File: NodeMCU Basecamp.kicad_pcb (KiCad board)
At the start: 2 copper layers, 71.1 x 53.3 mm, 60 parts, among them Q1 BSS138, Q10 BSS138, Q11 BSS138, Q12 BSS138, Q13 BSS138, Q2 BSS138, Q3 BSS138, Q4 BSS138, Q5 BSS138, Q6 BSS138, Q7 BSS138, Q8 BSS138, Q9 BSS138, U1 GND_BUS, U10 S_JUMPER_4, U11 S_JUMPER_4, U12 S_JUMPER_4, U13 S_JUMPER_4, U14 S_JUMPER_4, U15 S_JUMPER_4, U16 S_JUMPER_4, U17 S_JUMPER_4, U18 S_JUMPER_4, U19 S_JUMPER_4, U2 NODEMCU_AMICA, U3 DEV_PINS, U4 3V3_BUS, U5 5V_BUS, U6 S_JUMPER_4, U7 S_JUMPER_4, U8 S_JUMPER_4, U9 S_JUMPER_4

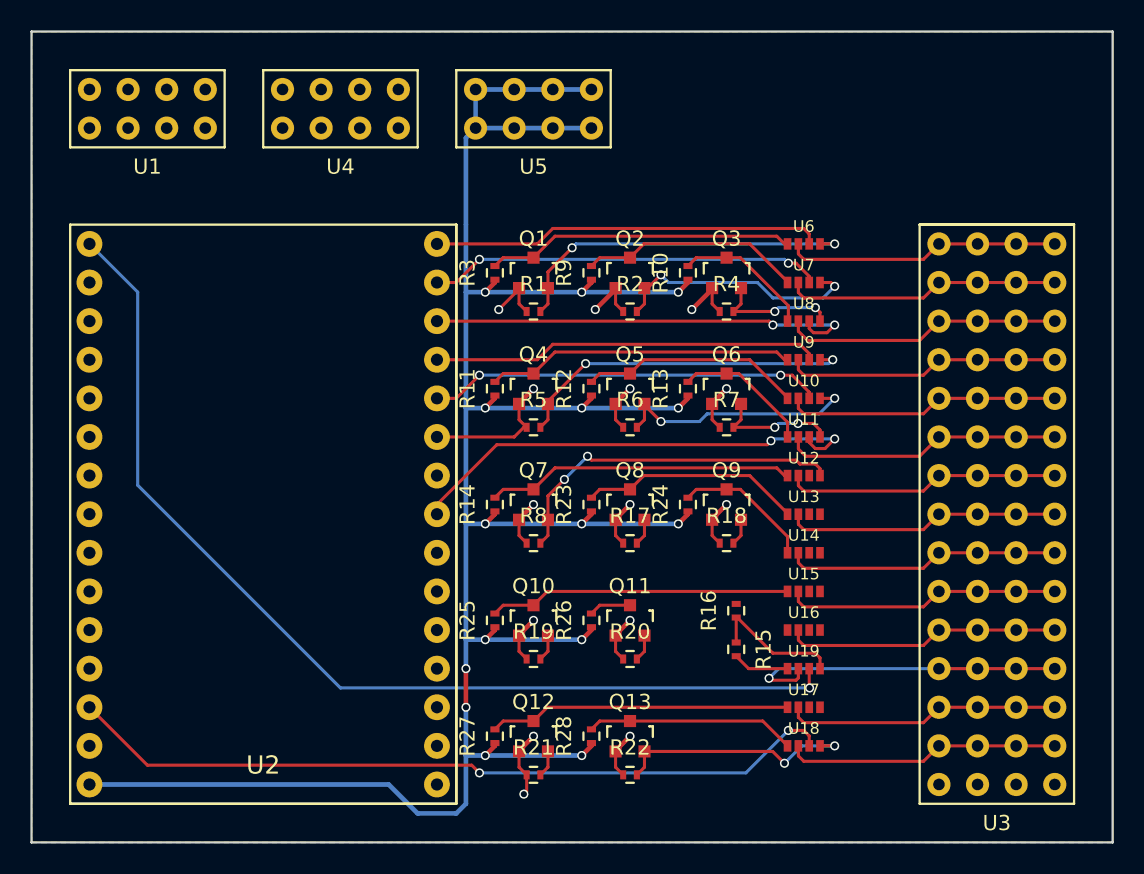
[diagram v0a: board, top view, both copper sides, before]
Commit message: rework: remove jumpers
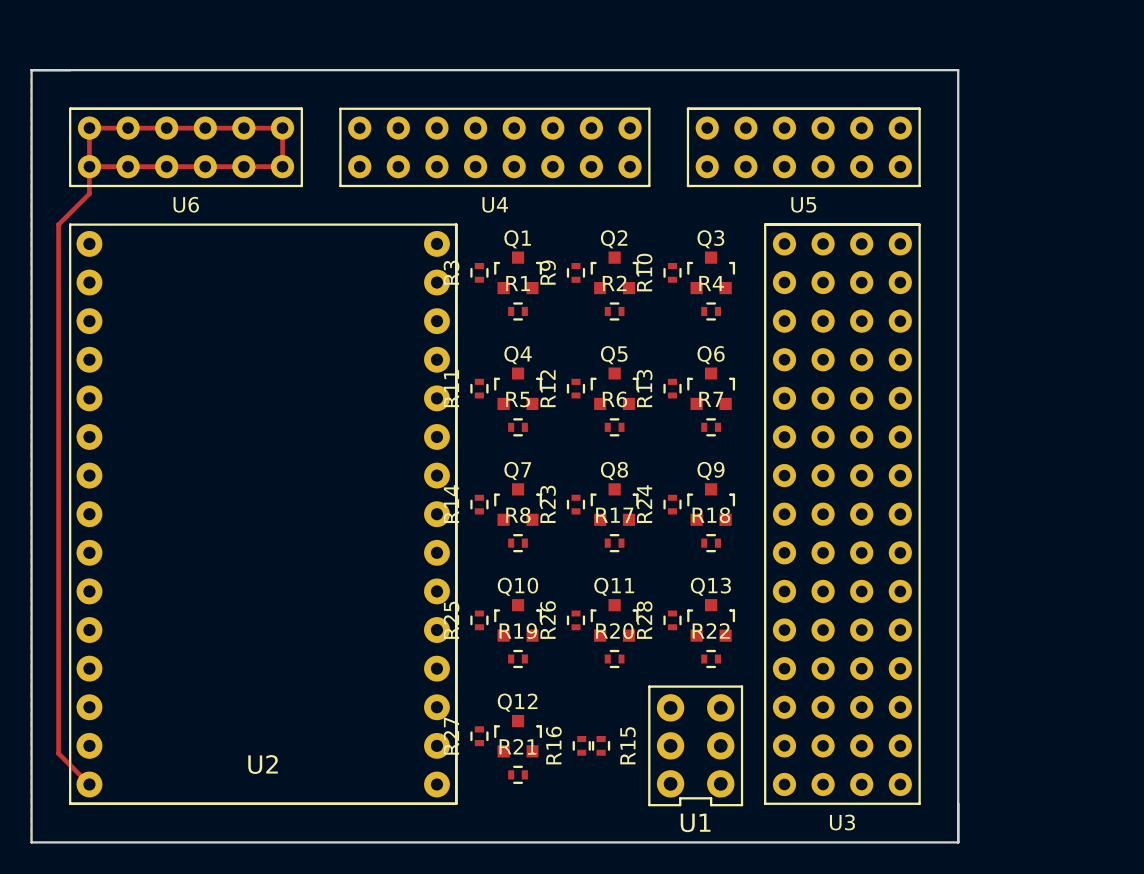
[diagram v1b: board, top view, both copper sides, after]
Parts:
- removed U10, U11, U12, U13, U14, U15, U16, U17, U18, U19, U7, U8, U9: S_JUMPER_4, mplewis:S_JUMPER_4
- Q1: footprint SOT-23 -> TO_SOT_Packages_SMD:SOT-23
- R15: value 33K -> 10K
- R16: value 68K -> 10K
- R21: value 10K -> 33K
- R22: value 10K -> 68K
- U1: value GND_BUS -> JS202011CQN; footprint mplewis:HEADER_BUS_4X2 -> mplewis:JS202011CQN
- U4: value 3V3_BUS -> GND_BUS; footprint mplewis:HEADER_BUS_4X2 -> mplewis:HEADER_BUS_4X8
- U5: value 5V_BUS -> 3V3_BUS; footprint mplewis:HEADER_BUS_4X2 -> mplewis:HEADER_BUS_4X6
- U6: value S_JUMPER_4 -> 5V_BUS; footprint mplewis:S_JUMPER_4 -> mplewis:HEADER_BUS_4X6
- moved U1 55.3 mm to (69.1, 69.8), turned to 180 degrees
- moved U6 41.1 mm to (35.6, 30.5)
- moved U5 18.0 mm to (76.2, 30.5)
- moved R16 13.5 mm to (61.6, 69.8)
- moved R15 10.9 mm to (62.9, 69.8)
- moved U4 10.5 mm to (55.9, 30.5)
- moved U3 10.2 mm to (78.7, 54.6)
- moved Q13 9.30 mm to (70.1, 61.6)
- moved R28 9.30 mm to (67.6, 61.6)
- moved R22 9.30 mm to (70.1, 64.1)
- moved Q3 1.02 mm to (70.1, 38.7)
- moved Q6 1.02 mm to (70.1, 46.4)
- moved Q9 1.02 mm to (70.1, 54.0)
- moved R10 1.02 mm to (67.6, 38.7)
- moved R11 1.02 mm to (54.9, 46.4)
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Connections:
- Q1 pad 2: D0_LV_LT -> D0_LV
- Q1 pad 3: D0_HV -> D0_XV
- Q10 pad 2: RX_LV_LT -> RX_LV
- Q10 pad 3: RX_HV -> RX_XV
- Q11 pad 2: TX_LV_LT -> TX_LV
- Q11 pad 3: TX_HV -> TX_XV
- Q12 pad 2: EN_LV_LT -> EN_LV
- Q12 pad 3: EN_HV -> EN_XV
- Q13 pad 2: RST_LV_LT -> RST_LV
- Q13 pad 3: RST_HV -> RST_XV
- Q2 pad 2: D1_LV_LT -> D1_LV
- Q2 pad 3: D1_HV -> D1_XV
- Q3 pad 2: D2_LV_LT -> D2_LV
- Q3 pad 3: D2_HV -> D2_XV
- Q4 pad 2: D3_LV_LT -> D3_LV
- Q4 pad 3: D3_HV -> D3_XV
- Q5 pad 2: D4_LV_LT -> D4_LV
- Q5 pad 3: D4_HV -> D4_XV
- Q6 pad 2: D5_LV_LT -> D5_LV
- Q6 pad 3: D5_HV -> D5_XV
- Q7 pad 2: D6_LV_LT -> D6_LV
- Q7 pad 3: D6_HV -> D6_XV
- Q8 pad 2: D7_LV_LT -> D7_LV
- Q8 pad 3: D7_HV -> D7_XV
- Q9 pad 2: D8_LV_LT -> D8_LV
- Q9 pad 3: D8_HV -> D8_XV
- R1 pad 2: D0_LV_LT -> D0_LV
- R10 pad 1: 5V -> OP_V
- R10 pad 2: D2_HV -> D2_XV
- R11 pad 1: 5V -> OP_V
- R11 pad 2: D3_HV -> D3_XV
- R12 pad 1: 5V -> OP_V
- R12 pad 2: D4_HV -> D4_XV
- R13 pad 1: 5V -> OP_V
- R13 pad 2: D5_HV -> D5_XV
- R14 pad 1: 5V -> OP_V
- R14 pad 2: D6_HV -> D6_XV
- R15 pad 1: A0_LV_LT -> 3V3
- R15 pad 2: A0_HV -> D7_LV
- R16 pad 1: A0_LV_LT -> 3V3
- R16 pad 2: GND -> D8_LV
- R17 pad 2: D7_LV_LT -> RX_LV
- R18 pad 2: D8_LV_LT -> TX_LV
- R19 pad 2: RX_LV_LT -> EN_LV
- R2 pad 2: D1_LV_LT -> D1_LV
- R20 pad 2: TX_LV_LT -> RST_LV
- R21 pad 1: 3V3 -> A0_LV_LT
- R21 pad 2: EN_LV_LT -> (no net)
- R22 pad 1: 3V3 -> A0_LV_LT
- R22 pad 2: RST_LV_LT -> Earth
- R23 pad 1: 5V -> OP_V
- R23 pad 2: D7_HV -> D7_XV
- R24 pad 1: 5V -> OP_V
- R24 pad 2: D8_HV -> D8_XV
- R25 pad 1: 5V -> OP_V
- R25 pad 2: RX_HV -> RX_XV
- R26 pad 1: 5V -> OP_V
- R26 pad 2: TX_HV -> TX_XV
- R27 pad 1: 5V -> OP_V
- R27 pad 2: EN_HV -> EN_XV
- R28 pad 1: 5V -> OP_V
- R28 pad 2: RST_HV -> RST_XV
- R3 pad 1: 5V -> 3V3
- R3 pad 2: D0_HV -> D2_LV
- R4 pad 2: D2_LV_LT -> D3_LV
- R5 pad 2: D3_LV_LT -> D4_LV
- R6 pad 2: D4_LV_LT -> D5_LV
- R7 pad 2: D5_LV_LT -> D6_LV
- R8 pad 1: 3V3 -> OP_V
- R8 pad 2: D6_LV_LT -> D0_XV
- R9 pad 1: 5V -> (no net)
- R9 pad 2: D1_HV -> D1_XV
- U1 pad 1: GND -> 3V3
- U2 pad 1: A0_LV -> (no net)
- U2 pad 10: GND -> Earth
- U2 pad 14: GND -> Earth
- U2 pad 17: GND -> Earth
- U2 pad 2: Net-(U2-Pad2) -> (no net)
- U2 pad 24: GND -> Earth
- U2 pad 3: Net-(U2-Pad3) -> (no net)
- U2 pad 4: Net-(U2-Pad4) -> (no net)
- U2 pad 5: Net-(U2-Pad5) -> (no net)
- U2 pad 6: Net-(U2-Pad6) -> (no net)
- U2 pad 7: Net-(U2-Pad7) -> (no net)
- U2 pad 8: Net-(U2-Pad8) -> (no net)
- U2 pad 9: Net-(U2-Pad9) -> (no net)
- U3 pad 15: GND -> Earth
- U4 pad 1: 3V3 -> Earth
- U5 pad 1: 5V -> 3V3
- U6 pad 1: D0_HV -> 5V
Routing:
- net 5V: track 159.5 -> 72.8 mm, vias 15 -> 0
- net A0_LV: track 68.2 -> 0.00 mm, vias 1 -> 0
- net RST_LV: track 51.1 -> 0.00 mm, vias 2 -> 0
- net 3V3: track 50.2 -> 0.00 mm, vias 14 -> 0
- net D5_LV: track 31.0 -> 0.00 mm, vias 2 -> 0
- net D2_LV: track 28.8 -> 0.00 mm, vias 2 -> 0
- net D4_LV: track 26.0 -> 0.00 mm, vias 2 -> 0
- net D1_LV: track 26.0 -> 0.00 mm, vias 2 -> 0
- net D0_LV: track 25.7 -> 0.00 mm
- net D3_LV: track 25.6 -> 0.00 mm
- net D0_LV_LT: track 23.4 -> 0.00 mm, vias 2 -> 0
- net D6_LV_LT: track 23.1 -> 0.00 mm, vias 2 -> 0
- net D3_LV_LT: track 22.6 -> 0.00 mm, vias 2 -> 0
- net A0_XV: track 21.7 -> 0.00 mm, vias 1 -> 0
- net D6_HV: track 20.3 -> 0.00 mm
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- added copper zone on F.Cu, net Earth
- removed copper zone on F.Cu, net GND
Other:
- board size 71.1 x 53.3 mm -> 61 x 50.8 mm

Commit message: pcb: LT wired to dev pins
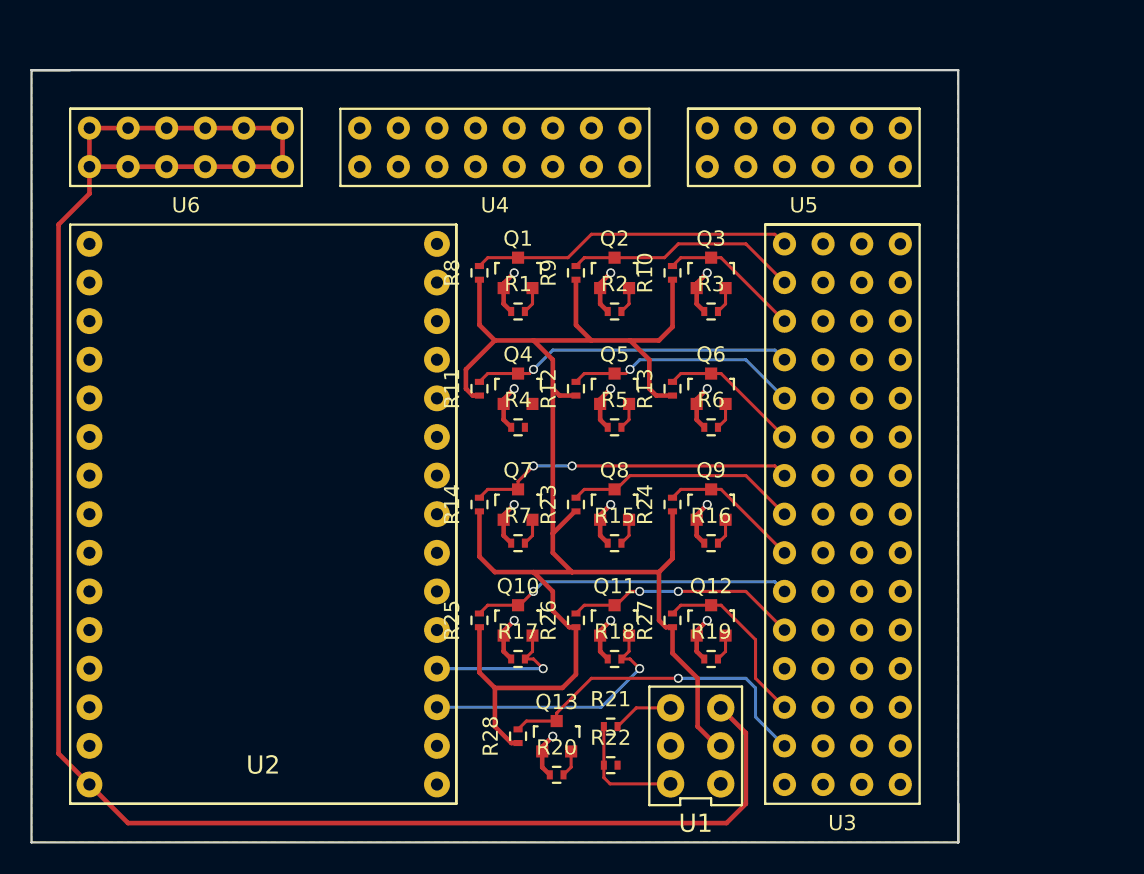
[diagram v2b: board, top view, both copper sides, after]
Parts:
- moved R8 18.0 mm to (54.9, 38.7), turned to 90 degrees
- moved R16 15.8 mm to (70.1, 56.5), turned to 0 degrees
- moved R3 15.5 mm to (70.1, 41.3), turned to 0 degrees
- moved Q12 14.8 mm to (70.1, 61.6)
- moved R27 14.8 mm to (67.6, 61.6)
- moved R4 14.8 mm to (57.4, 48.9)
- moved R7 14.8 mm to (57.4, 56.5)
- moved R15 13.4 mm to (63.8, 56.5), turned to 0 degrees
- moved Q13 12.7 mm to (59.9, 69.2)
- moved R19 12.7 mm to (70.1, 64.1)
- moved R28 12.7 mm to (57.4, 69.2)
- moved R18 9.92 mm to (63.8, 64.1)
- moved R17 9.92 mm to (57.4, 64.1)
- moved R22 9.61 mm to (63.5, 71.1)
- moved R20 8.52 mm to (59.9, 71.8)
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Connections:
- R21 pad 1: A0_LV_LT -> A0_STEPDOWN
- R21 pad 2: (no net) -> A0_XV
- R22 pad 1: A0_LV_LT -> A0_STEPDOWN
- R9 pad 1: (no net) -> OP_V
- U1 pad 4: (no net) -> A0_XV
- U1 pad 5: (no net) -> A0_LV
- U1 pad 6: (no net) -> A0_STEPDOWN
- U2 pad 1: (no net) -> A0_LV
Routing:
- net OP_V: track 0.00 -> 110.7 mm
- net 5V: track 72.8 -> 124.6 mm
- net 3V3: track 0.00 -> 39.6 mm, vias 0 -> 13
- net RST_XV: track 0.00 -> 22.2 mm, vias 0 -> 1
- net D6_XV: track 0.00 -> 21.5 mm, vias 0 -> 2
- net D3_XV: track 0.00 -> 21.2 mm, vias 0 -> 1
- net RX_XV: track 0.00 -> 21.2 mm, vias 0 -> 1
- net D0_XV: track 0.00 -> 21.2 mm
- net TX_LV: track 0.00 -> 17.6 mm, vias 0 -> 1
- net TX_XV: track 0.00 -> 15.4 mm, vias 0 -> 2
- net D7_XV: track 0.00 -> 15.4 mm
- net D4_XV: track 0.00 -> 15.4 mm, vias 0 -> 1
- net D1_XV: track 0.00 -> 15.4 mm
- net EN_XV: track 0.00 -> 11.9 mm
- net RX_LV: track 0.00 -> 10.2 mm, vias 0 -> 1
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
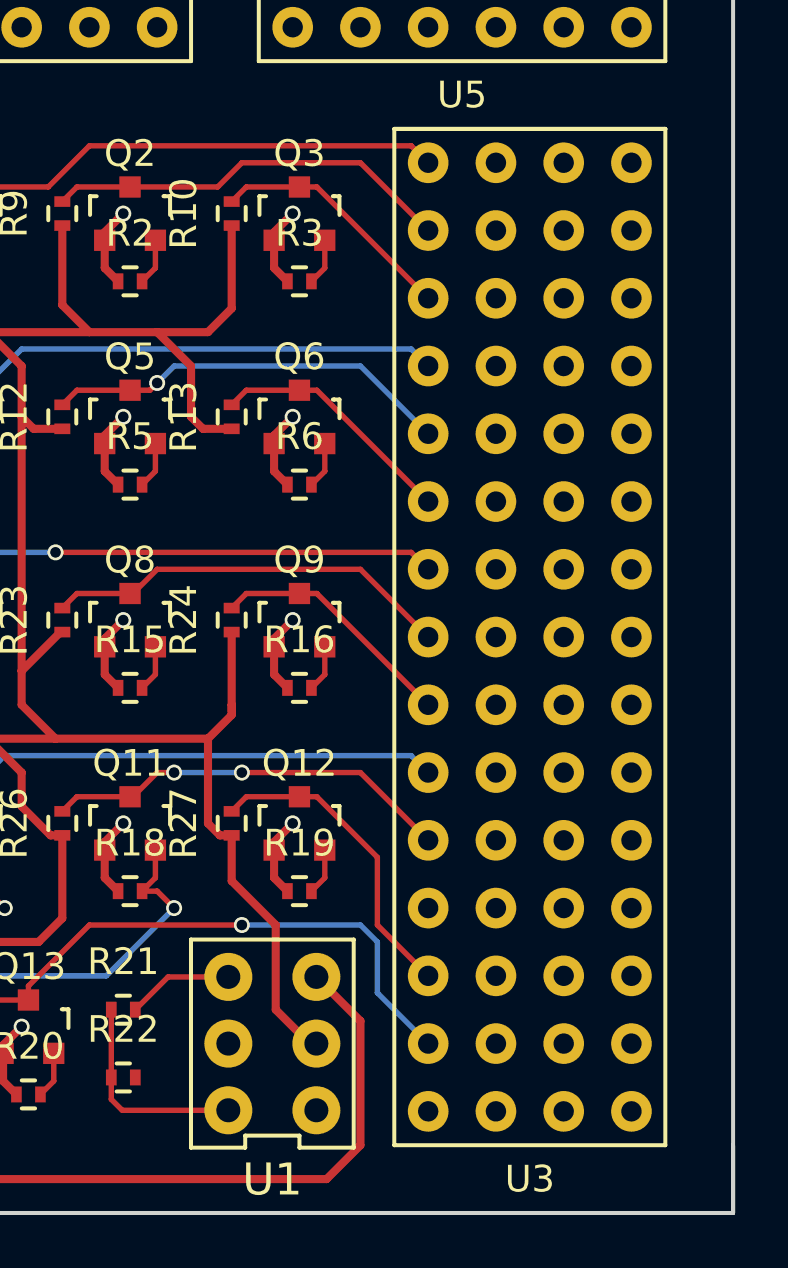
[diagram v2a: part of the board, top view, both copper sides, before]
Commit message: pcb: wired bus dev pins and floating gnd island
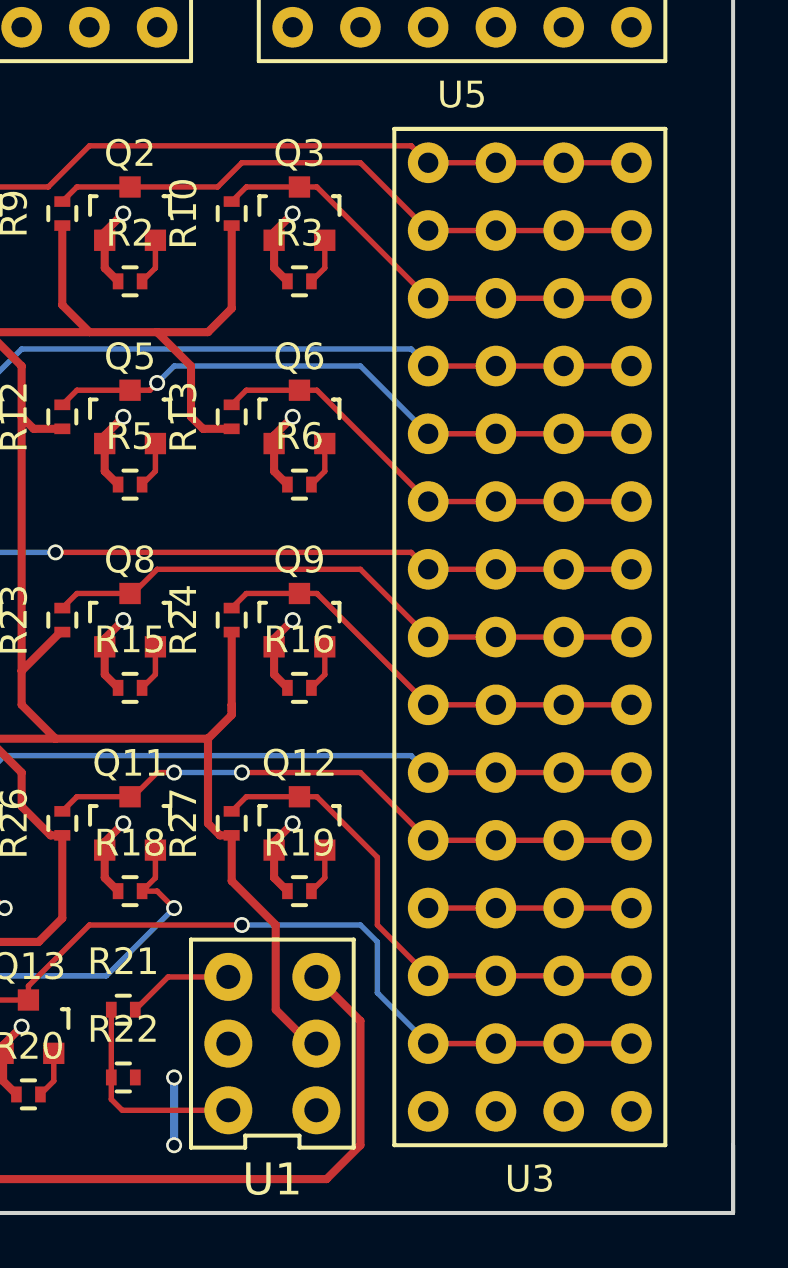
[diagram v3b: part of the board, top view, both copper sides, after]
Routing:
- net D1_XV: track 15.4 -> 23.0 mm
- net TX_XV: track 15.4 -> 23.0 mm
- net RX_XV: track 21.2 -> 28.8 mm
- net RST_XV: track 22.2 -> 29.8 mm
- net D8_XV: track 9.32 -> 16.9 mm
- net D7_XV: track 15.4 -> 23.0 mm
- net D6_XV: track 21.5 -> 29.1 mm
- net D5_XV: track 9.96 -> 17.6 mm
- net D4_XV: track 15.4 -> 23.0 mm
- net D3_XV: track 21.2 -> 28.8 mm
- net D2_XV: track 9.32 -> 16.9 mm
- net D0_XV: track 21.2 -> 28.8 mm
- net A0_XV: track 4.00 -> 11.6 mm
- net EN_XV: track 11.9 -> 19.5 mm
- net Earth: track 0.00 -> 2.54 mm, vias 0 -> 2

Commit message: pcb: first draft
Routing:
- net A0_LV: track 0.00 -> 57.9 mm
- net EN_LV: track 1.75 -> 46.3 mm, vias 0 -> 3
- net RST_LV: track 1.75 -> 37.3 mm
- net D8_LV: track 1.75 -> 23.3 mm, vias 0 -> 1
- net D5_LV: track 1.75 -> 23.3 mm, vias 0 -> 1
- net D2_LV: track 1.75 -> 21.4 mm, vias 0 -> 1
- net 3V3: track 39.6 -> 57.5 mm, vias 13 -> 15
- net D7_LV: track 1.75 -> 17.6 mm, vias 0 -> 1
- net D1_LV: track 1.75 -> 17.1 mm, vias 0 -> 1
- net D4_LV: track 1.75 -> 16.6 mm, vias 0 -> 1
- net Earth: track 2.54 -> 14.1 mm, vias 2 -> 4
- net D0_LV: track 1.75 -> 12.5 mm, vias 0 -> 1
- net D3_LV: track 0.00 -> 9.91 mm, vias 0 -> 1
- net A0_XV: track 11.6 -> 21.0 mm
- net D6_LV: track 1.75 -> 8.93 mm, vias 0 -> 1
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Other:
- board size 61 x 50.8 mm -> 63.5 x 50.8 mm
- rule pad_to_mask_clearance: 0.2 -> 0
- board text added: "20151227"
- board text added: "3.3V"
- board text added: "5V"
- board text added: "A0"
- board text added: "D0"
- board text added: "D1"
- board text added: "D2"
- board text added: "D3"
- board text added: "D4"
- board text added: "D5"
- board text added: "D6"
- board text added: "D7"
- board text added: "D8"
- board text added: "Designed for NodeMCU Amica"
- board text added: "EN"
- board text added: "GND"
- board text added: "NodeMCU Basecamp"
- board text added: "RST"
- board text added: "RX"
- board text added: "Rev. 1"
- board text added: "TX"
- board text added: "kesdev.com"
